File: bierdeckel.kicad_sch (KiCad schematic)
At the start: 30 parts, among them J1 Pogo, J2 Pogo, J3 Pogo, J4 Pogo, J6 USB4110-GF-A, Q1 BSS138P,215, SW1 PTS526 SK15 SMTR2 LFS, SW2 PTS526 SK15 SMTR2 LFS, SW3 PTS526 SK15 SMTR2 LFS, U1 ESP32-C3-WROOM-02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

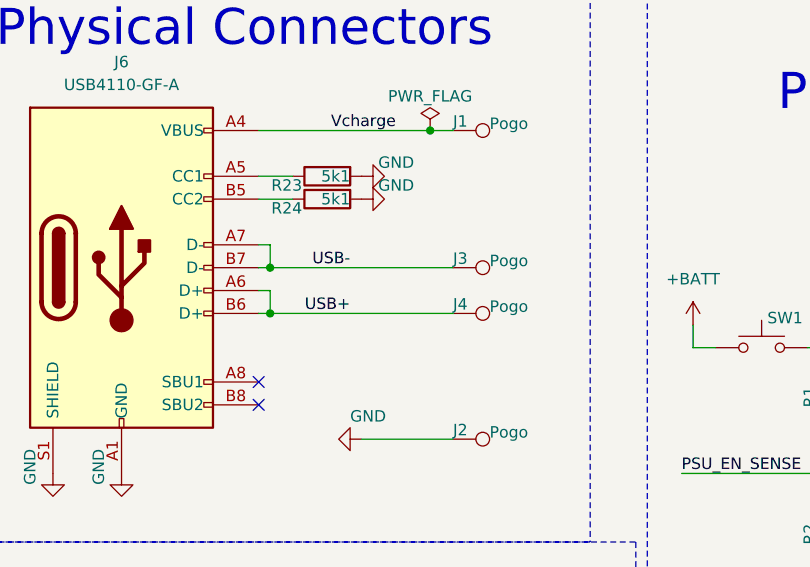
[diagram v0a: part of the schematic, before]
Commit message: add usb c connector
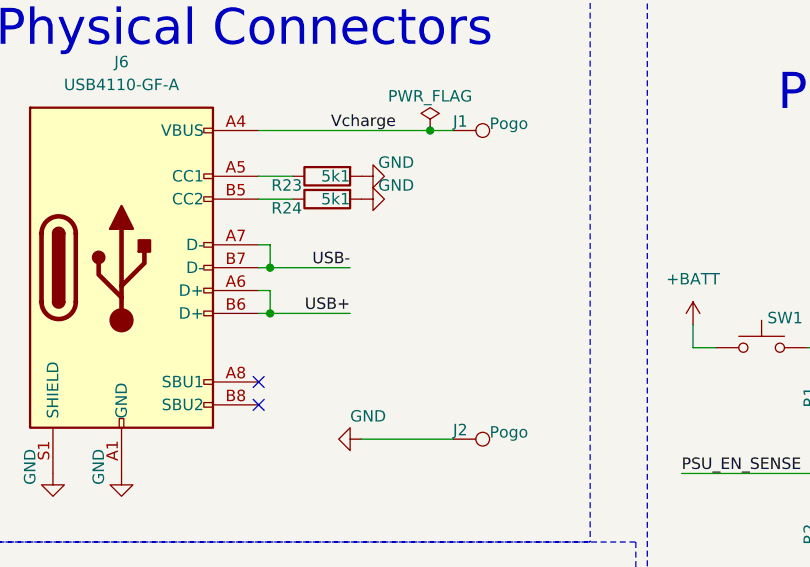
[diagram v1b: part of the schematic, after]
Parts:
- removed J3, J4: Pogo, TestPoint:TestPoint_Pad_D1.5mm, symbol Connector:TestPoint
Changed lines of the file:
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@@
 	)
 	(junction
-		(at 45.72 45.72)
+		(at 124.46 68.58)
 		(diameter 0)
 		(color 0 0 0 0)
 	)
 	(junction
-		(at 124.46 68.58)
+		(at 63.5 30.48)
 		(diameter 0)
 		(color 0 0 0 0)
 	)
 	(junction
-		(at 63.5 30.48)
+		(at 45.72 50.8)
 		(diameter 0)
 		(color 0 0 0 0)
@@
 	)
 	(junction
-		(at 45.72 50.8)
+		(at 210.82 45.72)
 		(diameter 0)
 		(color 0 0 0 0)
 	)
 	(junction
-		(at 210.82 45.72)
+		(at 224.79 53.34)
 		(diameter 0)
 		(color 0 0 0 0)
 	)
 	(junction
-		(at 224.79 53.34)
+		(at 45.72 45.72)
 		(diameter 0)
 		(color 0 0 0 0)
@@
 	(wire
 		(pts
+			(xy 45.72 45.72) (xy 54.61 45.72)
+		)
+		(stroke
+			(width 0)
+			(type default)
+		)
+	)
+	(wire
+		(pts
 			(xy 54.61 135.89) (xy 50.8 135.89)
 		)
@@
 	(wire
 		(pts
-			(xy 45.72 50.8) (xy 66.04 50.8)
-		)
-		(stroke
-			(width 0)
-			(type default)
-		)
-	)
-	(wire
-		(pts
 			(xy 238.76 80.01) (xy 255.27 80.01)
 		)
@@
 	(wire
 		(pts
-			(xy 243.84 143.51) (xy 233.68 143.51)
+			(xy 45.72 50.8) (xy 54.61 50.8)
 		)
 		(stroke
@@
 	(wire
 		(pts
-			(xy 248.92 74.93) (xy 238.76 74.93)
+			(xy 243.84 143.51) (xy 233.68 143.51)
 		)
 		(stroke
@@
 	(wire
 		(pts
-			(xy 45.72 45.72) (xy 66.04 45.72)
+			(xy 248.92 74.93) (xy 238.76 74.93)
 		)
 		(stroke
@@
 	)
 	(symbol
-		(lib_id "Connector:TestPoint")
-		(at 66.04 45.72 270)
-		(unit 1)
-		(exclude_from_sim no)
-		(in_bom no)
-		(on_board yes)
-		(dnp no)
-		(property "Reference" "J3"
-			(at 66.04 44.704 90)
-			(effects
-				(font
-					(size 1.27 1.27)
-				)
-				(justify left)
-			)
-		)
-		(property "Value" "Pogo"
-			(at 70.104 44.958 90)
-			(effects
-				(font
-					(size 1.27 1.27)
-				)
-				(justify left)
-			)
-		)
-		(property "Footprint" "TestPoint:TestPoint_Pad_D1.5mm"
-			(at 66.04 50.8 0)
-			(effects
-				(font
-					(size 1.27 1.27)
-				)
-				(hide yes)
-			)
-		)
-		(property "Datasheet" "https://www.digikey.at/en/products/detail/harwin-inc/S70-332002045R/6211252"
-			(at 66.04 50.8 0)
-			(effects
-				(font
-					(size 1.27 1.27)
-				)
-				(hide yes)
-			)
-		)
-		(property "Description" "test point"
-			(at 66.04 45.72 0)
-			(effects
-				(font
-					(size 1.27 1.27)
-				)
-				(hide yes)
-			)
-		)
-		(property "mpn" ""
-			(at 66.04 45.72 0)
-			(effects
-				(font
-					(size 1.27 1.27)
-				)
-				(hide yes)
-			)
-		)
-		(pin "1"
-		)
-		(instances
-			(project "bierdeckel"
-				(path "/a4ffe097-37ef-4e19-a91a-ae57f4a5aad1"
-					(reference "J3")
-					(unit 1)
-				)
-			)
-		)
-	)
-	(symbol
 		(lib_id "power:GND")
 		(at 107.95 83.82 0)
@@
 					(unit 1)
 				)
-			)
-		)
-	)
-	(symbol
-		(lib_id "Connector:TestPoint")
-		(at 66.04 50.8 270)
-		(unit 1)
-		(exclude_from_sim no)
-		(in_bom no)
-		(on_board yes)
-		(dnp no)
-		(property "Reference" "J4"
-			(at 66.04 49.784 90)
-			(effects
-				(font
-					(size 1.27 1.27)
-				)
-				(justify left)
-			)
-		)
-		(property "Value" "Pogo"
-			(at 70.104 50.038 90)
-			(effects
-				(font
-					(size 1.27 1.27)
-				)
-				(justify left)
-			)
-		)
-		(property "Footprint" "TestPoint:TestPoint_Pad_D1.5mm"
-			(at 66.04 55.88 0)
-			(effects
-				(font
-					(size 1.27 1.27)
-				)
-				(hide yes)
-			)
-		)
-		(property "Datasheet" "https://www.digikey.at/en/products/detail/harwin-inc/S70-332002045R/6211252"
-			(at 66.04 55.88 0)
-			(effects
-				(font
-					(size 1.27 1.27)
-				)
-				(hide yes)
-			)
-		)
-		(property "Description" "test point"
-			(at 66.04 50.8 0)
-			(effects
-				(font
-					(size 1.27 1.27)
-				)
-				(hide yes)
-			)
-		)
-		(property "mpn" ""
-			(at 66.04 50.8 0)
-			(effects
-				(font
-					(size 1.27 1.27)
-				)
-				(hide yes)
-			)
-		)
-		(pin "1"
-		)
-		(instances
-			(project "bierdeckel"
-				(path "/a4ffe097-37ef-4e19-a91a-ae57f4a5aad1"
-					(reference "J4")
-					(unit 1)
-				)

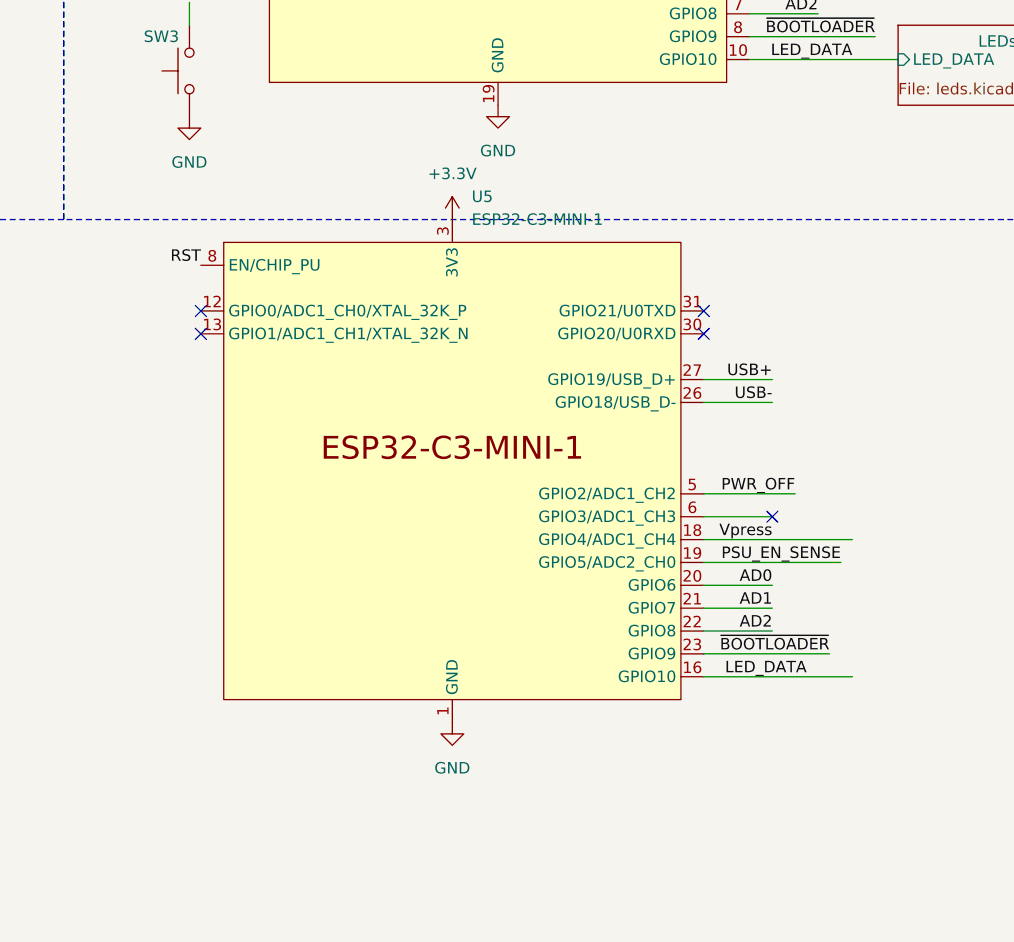
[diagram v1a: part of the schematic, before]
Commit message: remove excessive ESP mini
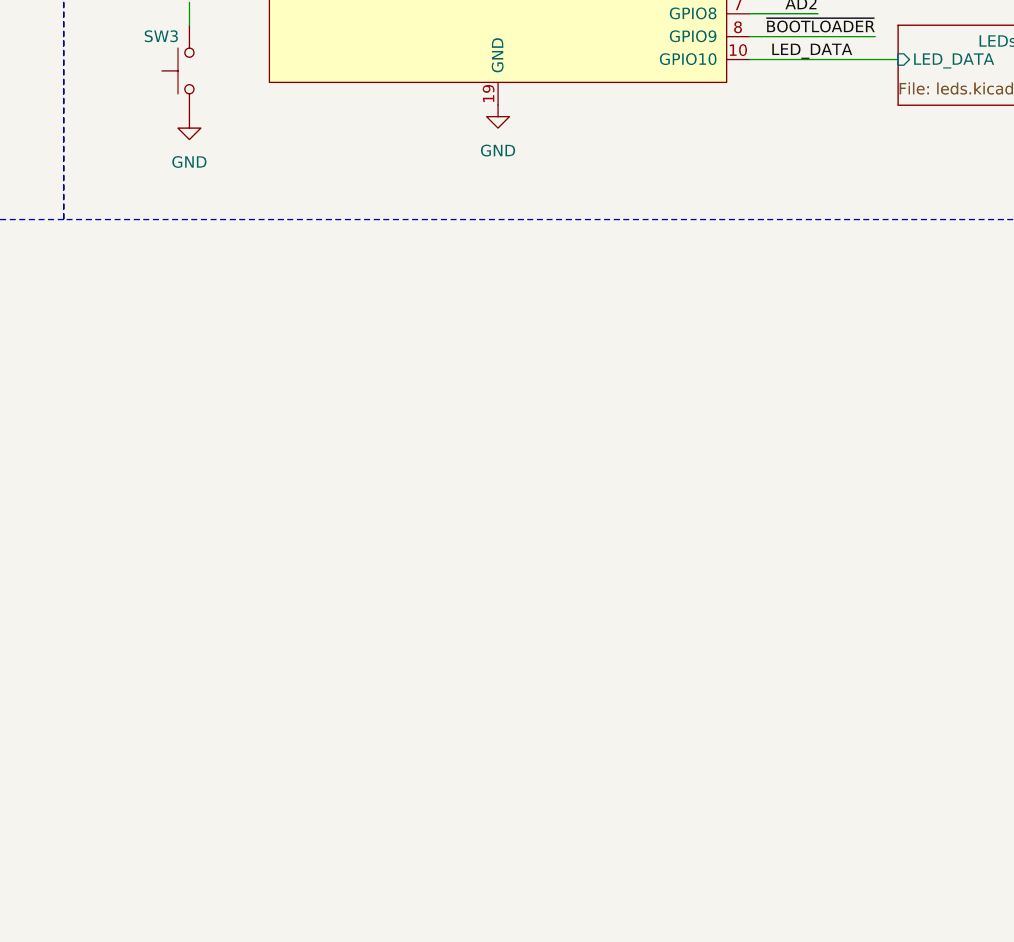
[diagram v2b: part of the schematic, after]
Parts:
- removed U5: ESP32-C3-MINI-1, PCM_Espressif:ESP32-C3-MINI-1, symbol PCM_Espressif:ESP32-C3-MINI-1
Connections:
- no-connect marks 12 -> 7

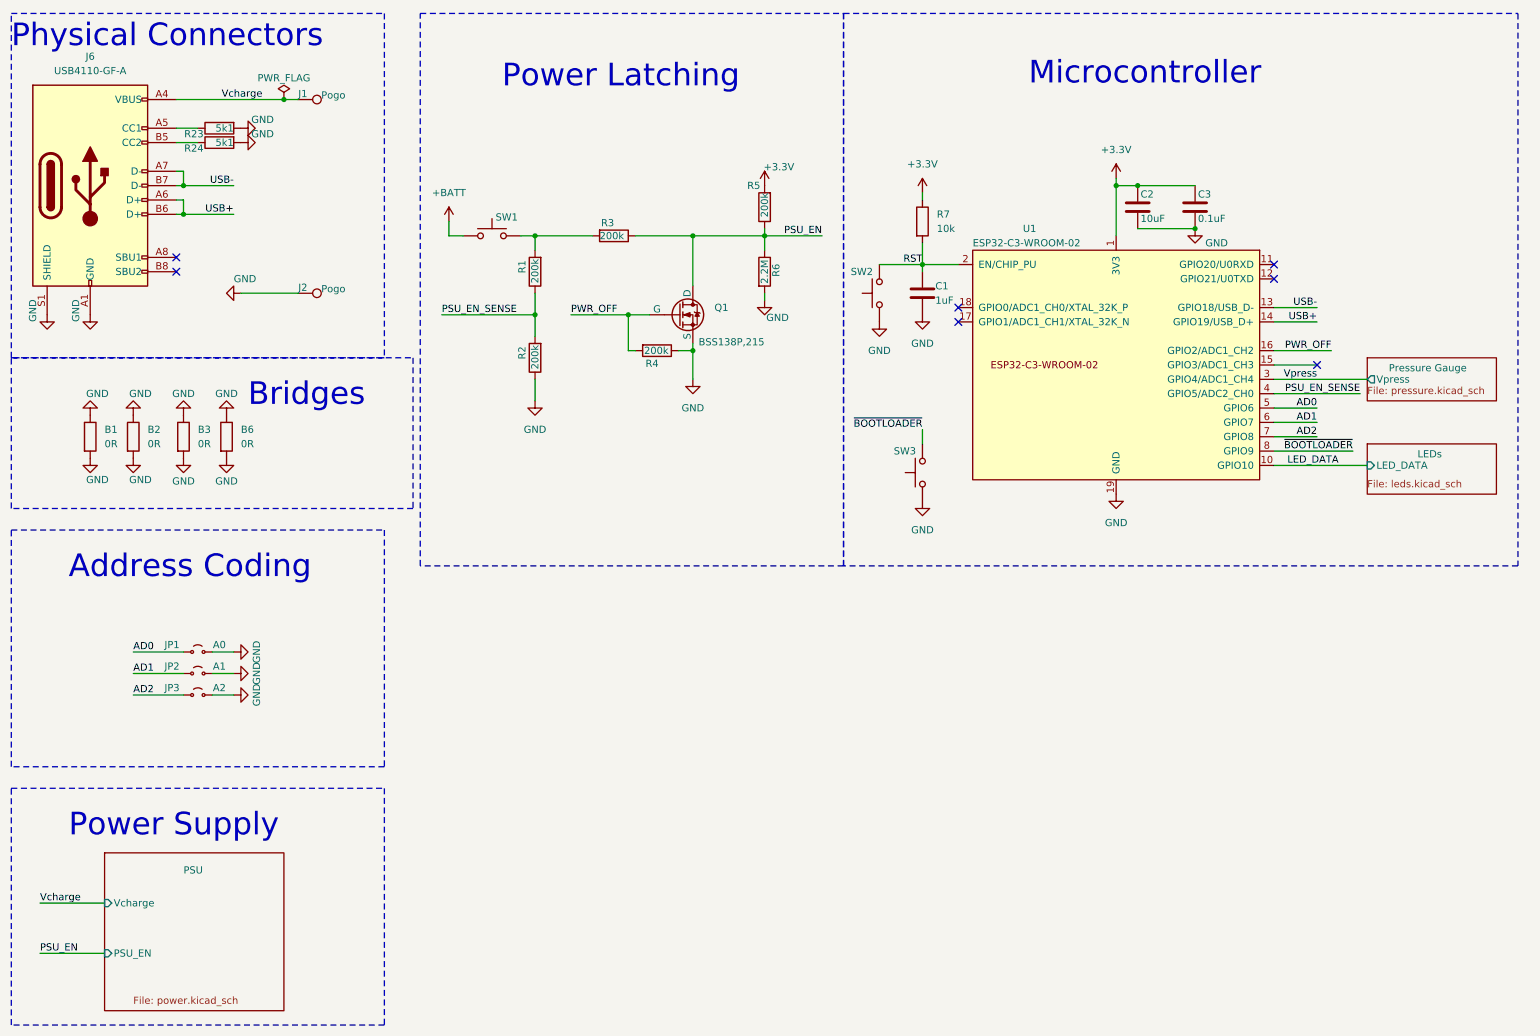
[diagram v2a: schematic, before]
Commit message: finish up routing and fix latching
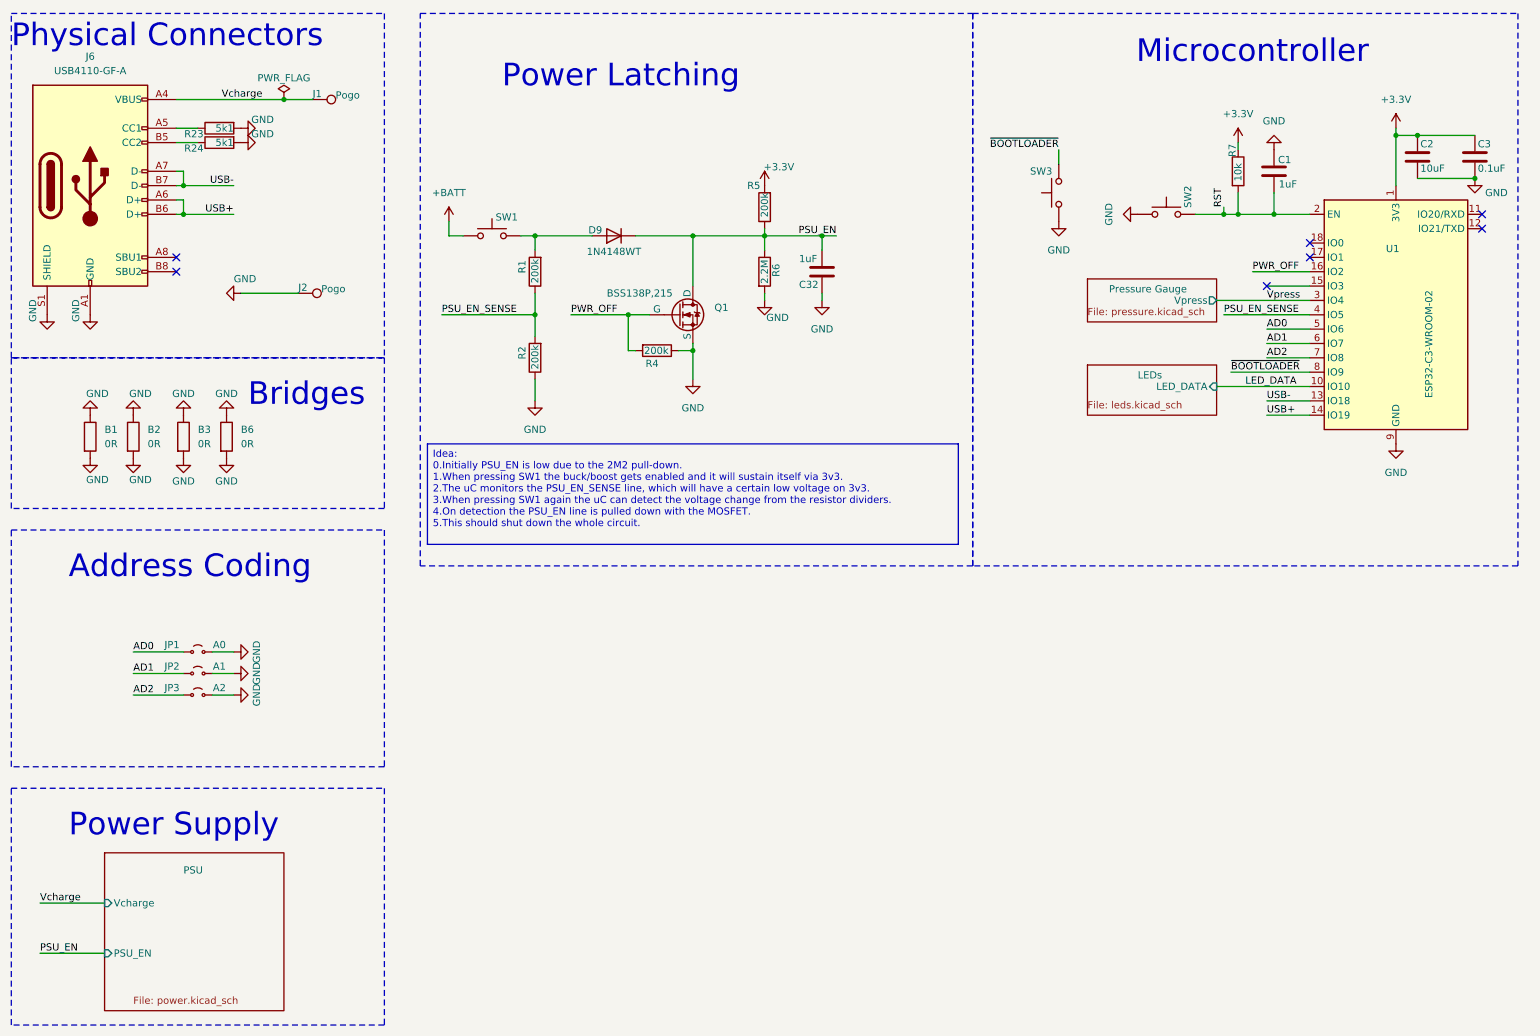
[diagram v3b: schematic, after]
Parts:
- removed R3: 200k, Resistor_SMD:R_0603_1608Metric, symbol Device:R
- removed U1: ESP32-C3-WROOM-02, PCM_Espressif:ESP32-C3-WROOM-02, symbol PCM_Espressif:ESP32-C3-WROOM-02
- added C32: 1uF, Capacitor_SMD:C_0805_2012Metric, symbol Device:C
- added D9: 1N4148WT, Diode_SMD:D_SOD-523, symbol Diode:1N4148WT
- added U1: ESP32-C3-WROOM-02, RF_Module:ESP32-C3-WROOM-02, symbol RF_Module:ESP32-C3-WROOM-02
- J1: footprint TestPoint:TestPoint_Pad_D3.0mm -> TestPoint:TestPoint_Pad_D1.5mm
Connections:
- net +3.3V: now also U1.1 (3V3)
- net AD0: now also U1.5 (IO6)
- net AD1: now also U1.6 (IO7)
- net AD2: now also U1.7 (IO8)
- net GND: now also C32.2, U1.19 (GND), U1.9 (GND)
- net LED_DATA: now also U1.10 (IO10)
- net PSU_EN: now also C32.1, D9.1 (K)
- net PSU_EN_SENSE: now also U1.4 (IO5)
- net PWR_OFF: now also U1.16 (IO2)
- net RST: now also U1.2 (EN)
- net USB+: now also U1.14 (IO19)
- net USB-: now also U1.13 (IO18)
- net Vpress: now also U1.3 (IO4)
- net ~{BOOTLOADER}: now also U1.8 (IO9)
- net at R1.2, SW1.2: now also D9.2 (A)
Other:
- moved on the sheet: C1, C2, C3, J1, R7, SW2, SW3

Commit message: replace some components for JLC order
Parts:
- D9: mpn (none) -> 1N4148WT
- JP1, JP2, JP3: now not fitted; now left out of the parts list
- Q1: mpn (none) -> BSS138P,215
- R1, R2, R4, R5: mpn CRCW08054K99FKEA -> (none)
- R23, R24, R7: mpn CR0805-FX-1002ELF -> (none)
- R6: mpn CRCW080562K0FKEA -> (none)
- U1: mpn (none) -> ESP32-C3-WROOM-02
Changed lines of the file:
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@@
 			)
 		)
-		(property "mpn" ""
+		(property "mpn" "BSS138P,215"
 			(at 133.35 68.58 0)
 			(effects
@@
 			)
 		)
-		(property "mpn" "CR0805-FX-1002ELF "
+		(property "mpn" ""
 			(at 52.07 35.56 0)
 			(effects
@@
 			)
 		)
-		(property "mpn" "CRCW08054K99FKEA"
+		(property "mpn" ""
 			(at 129.54 74.93 0)
 			(effects
@@
 			)
 		)
+		(property "mpn" "ESP32-C3-WROOM-02"
+			(at 260.35 68.58 0)
+			(effects
+				(font
+					(size 1.27 1.27)
+				)
+				(hide yes)
+			)
+		)
 		(pin "3"
 		)
@@
 		(unit 1)
 		(exclude_from_sim no)
-		(in_bom yes)
+		(in_bom no)
 		(on_board yes)
-		(dnp no)
+		(dnp yes)
 		(property "Reference" "JP1"
 			(at 43.688 127 0)
@@
 			)
 		)
-		(property "mpn" "CRCW08054K99FKEA"
+		(property "mpn" ""
 			(at 107.95 76.2 0)
 			(effects
@@
 			)
 		)
-		(property "mpn" "CRCW08054K99FKEA"
+		(property "mpn" ""
 			(at 107.95 60.96 0)
 			(effects
@@
 			)
 		)
-		(property "mpn" "CR0805-FX-1002ELF "
+		(property "mpn" ""
 			(at 52.07 38.1 0)
 			(effects
@@
 		(unit 1)
 		(exclude_from_sim no)
-		(in_bom yes)
+		(in_bom no)
 		(on_board yes)
-		(dnp no)
+		(dnp yes)
 		(property "Reference" "JP3"
 			(at 43.688 134.62 0)
@@
 			)
 		)
-		(property "mpn" "CRCW080562K0FKEA"
+		(property "mpn" ""
 			(at 148.59 60.96 0)
 			(effects
@@
 			)
 		)
+		(property "mpn" "1N4148WT"
+			(at 121.92 54.61 0)
+			(effects
+				(font
+					(size 1.27 1.27)
+				)
+				(hide yes)
+			)
+		)
 		(pin "1"
 		)
@@
 			)
 		)
-		(property "mpn" "CRCW08054K99FKEA"
+		(property "mpn" ""
 			(at 148.59 49.53 0)
 			(effects
@@
 			)
 		)
-		(property "mpn" "CR0805-FX-1002ELF "
+		(property "mpn" ""
 			(at 232.41 43.18 0)
 			(effects
@@
 		(unit 1)
 		(exclude_from_sim no)
-		(in_bom yes)
+		(in_bom no)
 		(on_board yes)
-		(dnp no)
+		(dnp yes)
 		(property "Reference" "JP2"
 			(at 43.688 130.81 0)

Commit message: change some more components to LCSC ones
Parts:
- J6: value USB4110-GF-A -> USB-TYPE-C-020; mpn USB4110-GF-A -> C2927040
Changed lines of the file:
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@@
 			)
 		)
-		(property "Value" "USB4110-GF-A"
+		(property "Value" "USB-TYPE-C-020"
 			(at 29.21 25.4 0)
 			(effects
@@
 			)
 		)
-		(property "mpn" "USB4110-GF-A"
+		(property "mpn" "C2927040"
 			(at 29.21 45.72 0)
 			(effects
